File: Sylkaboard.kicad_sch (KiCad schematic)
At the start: 117 parts, among them J1 Conn_01x04_Pin, J2 USB_C_Receptacle_USB2.0_16P, U1 RP2040-ZERO

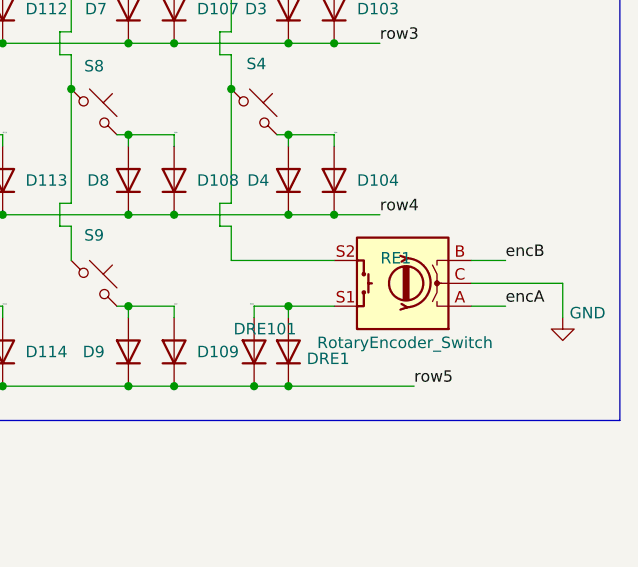
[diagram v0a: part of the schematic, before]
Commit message: swap usb-c connector and rotary encoder
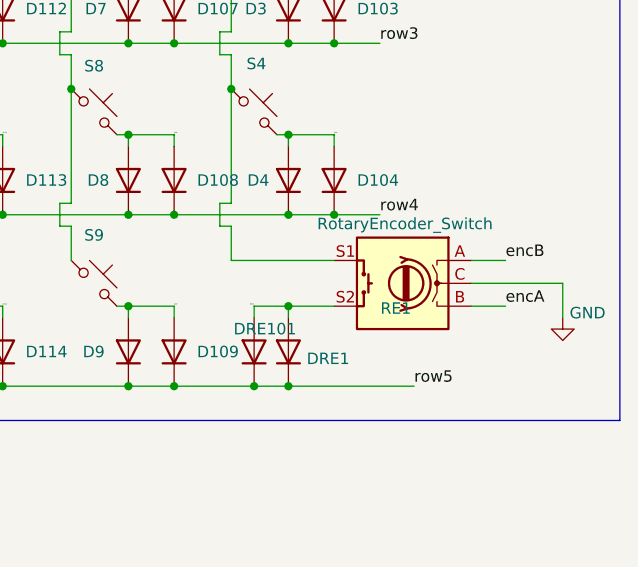
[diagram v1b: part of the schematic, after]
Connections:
- net RED1: now also RE1.S2; no longer RE1.S1
- net col6: now also RE1.S1; no longer RE1.S2
- net encA: now also RE1.B; no longer RE1.A
- net encB: now also RE1.A; no longer RE1.B
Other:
- moved on the sheet: RE1
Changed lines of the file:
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@@
 	(symbol
 		(lib_id "Device:RotaryEncoder_Switch")
-		(at 259.08 107.95 180)
+		(at 259.08 107.95 0)
+		(mirror y)
 		(unit 1)
 		(body_style 1)
@@
 		(dnp no)
 		(property "Reference" "RE1"
-			(at 258.318 105.156 0)
+			(at 258.318 110.744 0)
 			(show_name no)
 			(do_not_autoplace no)
@@
 		)
 		(property "Value" "RotaryEncoder_Switch"
-			(at 259.334 114.554 0)
+			(at 259.334 101.346 0)
 			(show_name no)
 			(do_not_autoplace no)
@@
 		)
 		(property "Footprint" "Rotary_Encoder:RotaryEncoder_Alps_EC11E-Switch_Vertical_H20mm"
-			(at 262.89 112.014 0)
+			(at 262.89 103.886 0)
 			(hide yes)
 			(show_name no)
@@
 		)
 		(property "Datasheet" ""
-			(at 259.08 114.554 0)
+			(at 259.08 101.346 0)
 			(hide yes)
 			(show_name no)

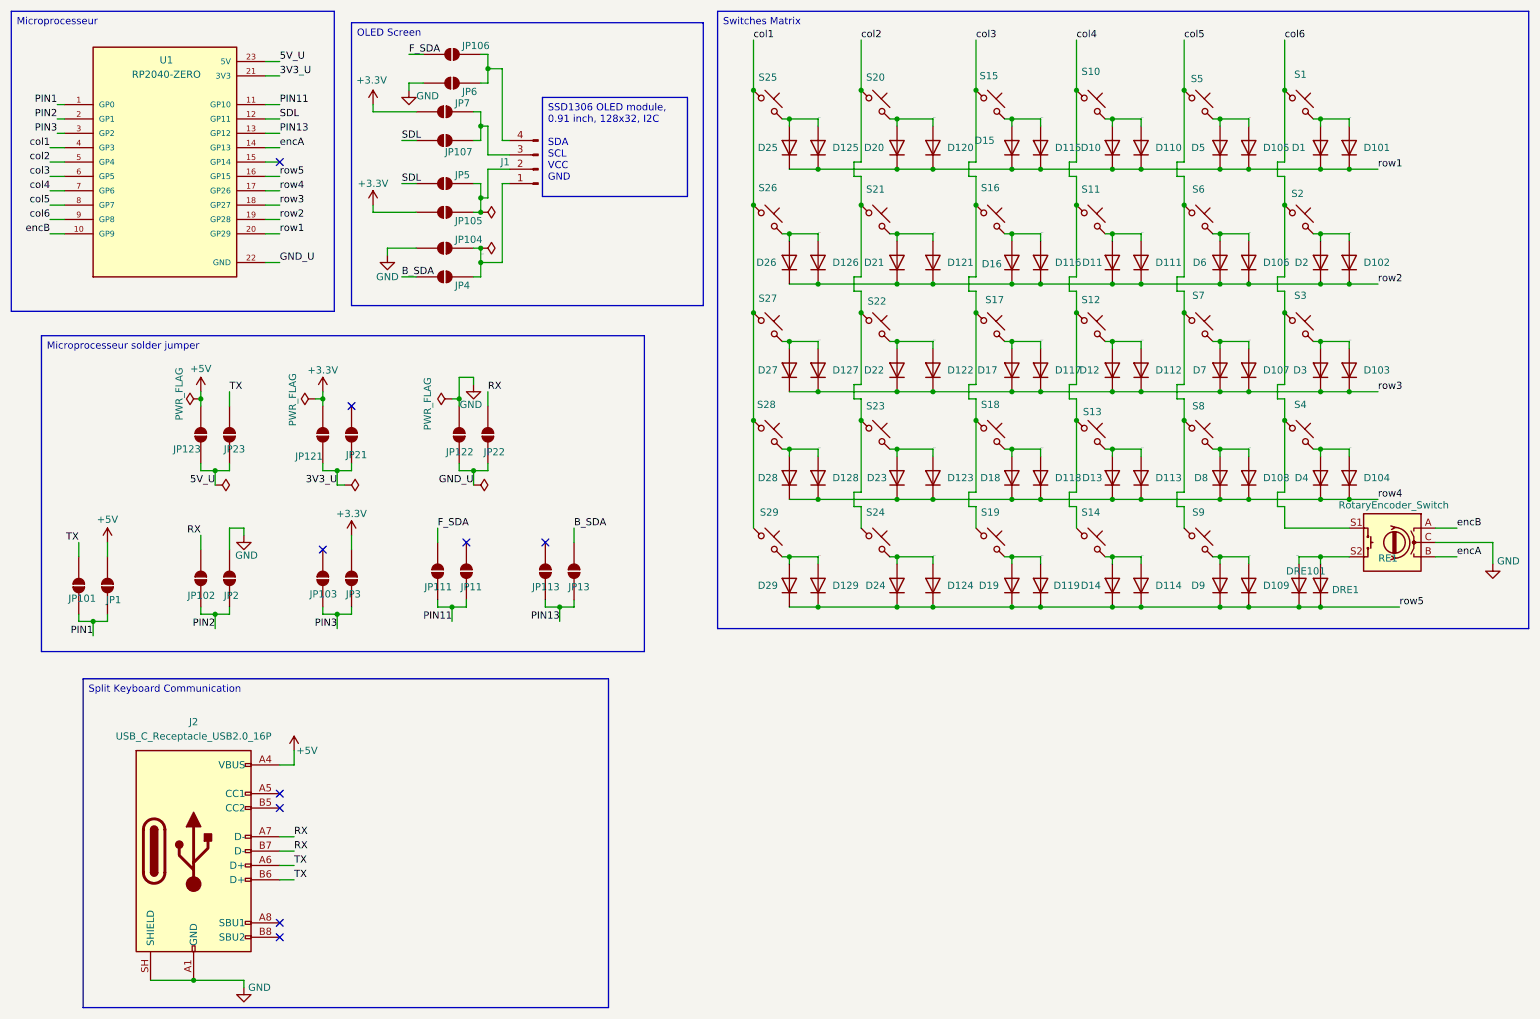
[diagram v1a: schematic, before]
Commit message: inverted encoder pins (A and B) on schematic
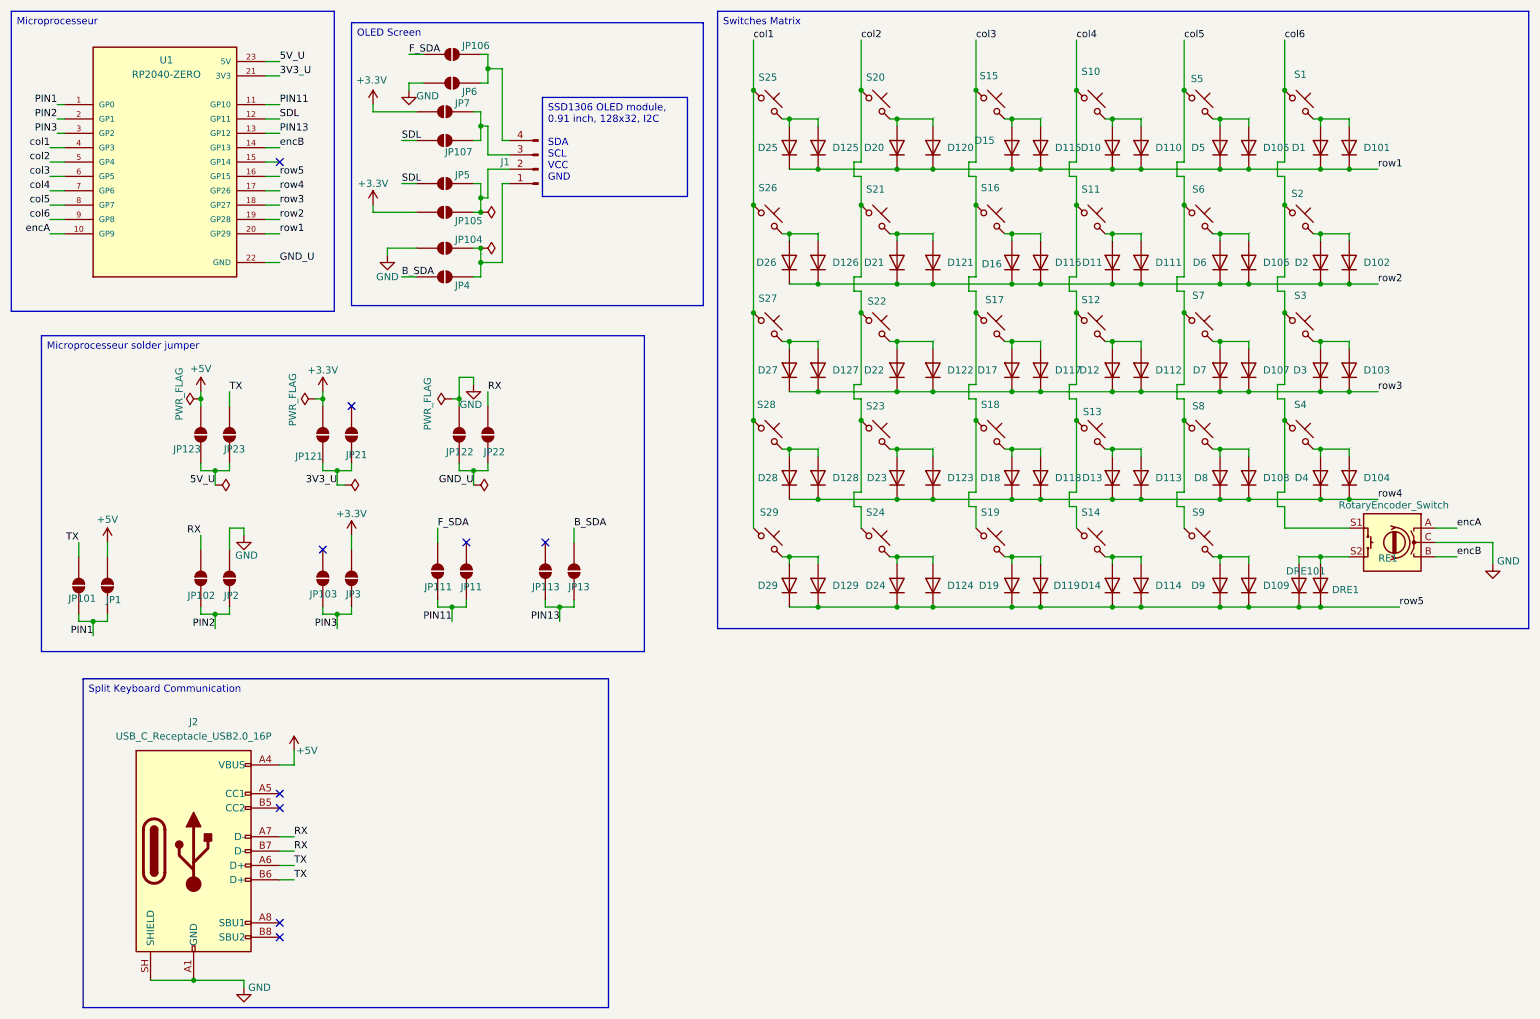
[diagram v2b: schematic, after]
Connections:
- net encA: now also RE1.A, U1.10 (GP9); no longer RE1.B, U1.14 (GP13)
- net encB: now also RE1.B, U1.14 (GP13); no longer RE1.A, U1.10 (GP9)
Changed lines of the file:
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@@
 		)
 	)
-	(label "encA"
+	(label "encB"
 		(at 270.51 110.49 0)
 		(effects
@@
 		)
 	)
-	(label "encB"
+	(label "encA"
 		(at 270.51 105.41 0)
 		(effects
@@
 		)
 	)
-	(label "encA"
+	(label "encB"
 		(at 62.23 38.1 0)
 		(effects
@@
 		)
 	)
-	(label "encB"
+	(label "encA"
 		(at 21.59 53.34 180)
 		(effects

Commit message: rx tx of the same length
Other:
- company: Pablo Berton -> Sylkaron
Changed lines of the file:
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@@
 		(date "2026-09-18")
 		(rev "v1.2")
-		(company "Pablo Berton")
+		(company "Sylkaron")
 	)
 	(text_box "Split Keyboard Communication"

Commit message: change switch footprint to a correct dimension holes
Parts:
- S1, S10, S11, S12, S13, S14, S15, S16, S17, S18, S19, S2, S20, S21, S22, S23, S24, S25, S26, S27, S28, S29, S3, S4, S5, S6, S7, S8, S9: footprint Footprints:Kailh_socket_PG1350_reversible -> Footprints:Kail_Hotswap_Reversible_V1V2
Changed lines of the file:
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@@
 			)
 		)
-		(property "Footprint" "Footprints:Kailh_socket_PG1350_reversible"
+		(property "Footprint" "Footprints:Kail_Hotswap_Reversible_V1V2"
 			(at 187.96 107.95 0)
 			(hide yes)
@@
 			)
 		)
-		(property "Footprint" "Footprints:Kailh_socket_PG1350_reversible"
+		(property "Footprint" "Footprints:Kail_Hotswap_Reversible_V1V2"
 			(at 148.59 30.48 0)
 			(hide yes)
@@
 			)
 		)
-		(property "Footprint" "Footprints:Kailh_socket_PG1350_reversible"
+		(property "Footprint" "Footprints:Kail_Hotswap_Reversible_V1V2"
 			(at 167.64 50.8 0)
 			(hide yes)
@@
 			)
 		)
-		(property "Footprint" "Footprints:Kailh_socket_PG1350_reversible"
+		(property "Footprint" "Footprints:Kail_Hotswap_Reversible_V1V2"
 			(at 187.96 69.85 0)
 			(hide yes)
@@
 			)
 		)
-		(property "Footprint" "Footprints:Kailh_socket_PG1350_reversible"
+		(property "Footprint" "Footprints:Kail_Hotswap_Reversible_V1V2"
 			(at 148.59 88.9 0)
 			(hide yes)
@@
 			)
 		)
-		(property "Footprint" "Footprints:Kailh_socket_PG1350_reversible"
+		(property "Footprint" "Footprints:Kail_Hotswap_Reversible_V1V2"
 			(at 205.74 69.85 0)
 			(hide yes)
@@
 			)
 		)
-		(property "Footprint" "Footprints:Kailh_socket_PG1350_reversible"
+		(property "Footprint" "Footprints:Kail_Hotswap_Reversible_V1V2"
 			(at 148.59 107.95 0)
 			(hide yes)
@@
 			)
 		)
-		(property "Footprint" "Footprints:Kailh_socket_PG1350_reversible"
+		(property "Footprint" "Footprints:Kail_Hotswap_Reversible_V1V2"
 			(at 224.79 69.85 0)
 			(hide yes)
@@
 			)
 		)
-		(property "Footprint" "Footprints:Kailh_socket_PG1350_reversible"
+		(property "Footprint" "Footprints:Kail_Hotswap_Reversible_V1V2"
 			(at 205.74 107.95 0)
 			(hide yes)
@@
 			)
 		)
-		(property "Footprint" "Footprints:Kailh_socket_PG1350_reversible"
+		(property "Footprint" "Footprints:Kail_Hotswap_Reversible_V1V2"
 			(at 224.79 107.95 0)
 			(hide yes)
@@
 			)
 		)
-		(property "Footprint" "Footprints:Kailh_socket_PG1350_reversible"
+		(property "Footprint" "Footprints:Kail_Hotswap_Reversible_V1V2"
 			(at 242.57 30.48 0)
 			(hide yes)
@@
 			)
 		)
-		(property "Footprint" "Footprints:Kailh_socket_PG1350_reversible"
+		(property "Footprint" "Footprints:Kail_Hotswap_Reversible_V1V2"
 			(at 187.96 30.48 0)
 			(hide yes)
@@
 			)
 		)
-		(property "Footprint" "Footprints:Kailh_socket_PG1350_reversible"
+		(property "Footprint" "Footprints:Kail_Hotswap_Reversible_V1V2"
 			(at 148.59 50.8 0)
 			(hide yes)
@@
 			)
 		)
-		(property "Footprint" "Footprints:Kailh_socket_PG1350_reversible"
+		(property "Footprint" "Footprints:Kail_Hotswap_Reversible_V1V2"
 			(at 242.57 50.8 0)
 			(hide yes)
@@
 			)
 		)
-		(property "Footprint" "Footprints:Kailh_socket_PG1350_reversible"
+		(property "Footprint" "Footprints:Kail_Hotswap_Reversible_V1V2"
 			(at 205.74 50.8 0)
 			(hide yes)
@@
 			)
 		)
-		(property "Footprint" "Footprints:Kailh_socket_PG1350_reversible"
+		(property "Footprint" "Footprints:Kail_Hotswap_Reversible_V1V2"
 			(at 167.64 69.85 0)
 			(hide yes)
@@
 			)
 		)
-		(property "Footprint" "Footprints:Kailh_socket_PG1350_reversible"
+		(property "Footprint" "Footprints:Kail_Hotswap_Reversible_V1V2"
 			(at 242.57 69.85 0)
 			(hide yes)
@@
 			)
 		)
-		(property "Footprint" "Footprints:Kailh_socket_PG1350_reversible"
+		(property "Footprint" "Footprints:Kail_Hotswap_Reversible_V1V2"
 			(at 205.74 88.9 0)
 			(hide yes)
@@
 			)
 		)
-		(property "Footprint" "Footprints:Kailh_socket_PG1350_reversible"
+		(property "Footprint" "Footprints:Kail_Hotswap_Reversible_V1V2"
 			(at 224.79 30.48 0)
 			(hide yes)
@@
 			)
 		)
-		(property "Footprint" "Footprints:Kailh_socket_PG1350_reversible"
+		(property "Footprint" "Footprints:Kail_Hotswap_Reversible_V1V2"
 			(at 205.74 30.48 0)
 			(hide yes)
@@
 			)
 		)
-		(property "Footprint" "Footprints:Kailh_socket_PG1350_reversible"
+		(property "Footprint" "Footprints:Kail_Hotswap_Reversible_V1V2"
 			(at 187.96 88.9 0)
 			(hide yes)
@@
 			)
 		)
-		(property "Footprint" "Footprints:Kailh_socket_PG1350_reversible"
+		(property "Footprint" "Footprints:Kail_Hotswap_Reversible_V1V2"
 			(at 167.64 107.95 0)
 			(hide yes)
@@
 			)
 		)
-		(property "Footprint" "Footprints:Kailh_socket_PG1350_reversible"
+		(property "Footprint" "Footprints:Kail_Hotswap_Reversible_V1V2"
 			(at 167.64 30.48 0)
 			(hide yes)
@@
 			)
 		)
-		(property "Footprint" "Footprints:Kailh_socket_PG1350_reversible"
+		(property "Footprint" "Footprints:Kail_Hotswap_Reversible_V1V2"
 			(at 224.79 88.9 0)
 			(hide yes)
@@
 			)
 		)
-		(property "Footprint" "Footprints:Kailh_socket_PG1350_reversible"
+		(property "Footprint" "Footprints:Kail_Hotswap_Reversible_V1V2"
 			(at 187.96 50.8 0)
 			(hide yes)
@@
 			)
 		)
-		(property "Footprint" "Footprints:Kailh_socket_PG1350_reversible"
+		(property "Footprint" "Footprints:Kail_Hotswap_Reversible_V1V2"
 			(at 242.57 88.9 0)
 			(hide yes)
@@
 			)
 		)
-		(property "Footprint" "Footprints:Kailh_socket_PG1350_reversible"
+		(property "Footprint" "Footprints:Kail_Hotswap_Reversible_V1V2"
 			(at 167.64 88.9 0)
 			(hide yes)
@@
 			)
 		)
-		(property "Footprint" "Footprints:Kailh_socket_PG1350_reversible"
+		(property "Footprint" "Footprints:Kail_Hotswap_Reversible_V1V2"
 			(at 148.59 69.85 0)
 			(hide yes)
@@
 			)
 		)
-		(property "Footprint" "Footprints:Kailh_socket_PG1350_reversible"
+		(property "Footprint" "Footprints:Kail_Hotswap_Reversible_V1V2"
 			(at 224.79 50.8 0)
 			(hide yes)
